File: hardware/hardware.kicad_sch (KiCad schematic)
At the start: 126 parts, among them J1 Conn_01x04_Pin, J2 Conn_01x04_Pin, J3 Conn_01x04_Pin, J4 Conn_01x04_Pin, J5 Conn_01x04_Pin, J6 Conn_01x04_Pin, J7 Conn_01x04_Pin, U1 DRV8825PWPR, U2 DRV8825PWPR, U3 DRV8825PWPR, U4 DRV8825PWPR, U5 DRV8825PWPR, U6 DRV8825PWPR, U7 DRV8825PWPR

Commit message: add relay + mcu schematic
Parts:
- removed C16, C20: 100n, Capacitor_SMD:CP_Elec_6.3x5.7, symbol Device:C_Polarized
- removed C22: 0.1u, Capacitor_SMD:C_0603_1608Metric, symbol Device:C_Small
- removed C23: 0.47u, Capacitor_SMD:C_0603_1608Metric, symbol Device:C_Small
- removed TP1, TP10, TP11, TP12, TP13, TP14, TP15, TP16, TP17, TP18, TP19, TP2, TP20, TP21, TP22, TP23, TP24, TP25, TP26, TP27, TP28, TP3, TP4, TP5, TP6, TP7, TP8, TP9: TestPoint, TestPoint:TestPoint_Pad_1.5x1.5mm, symbol Connector:TestPoint
- added C16: 0.1u, Capacitor_SMD:C_0603_1608Metric, symbol Device:C_Small
- added C20: 0.47u, Capacitor_SMD:C_0603_1608Metric, symbol Device:C_Small
- added C22, C23: 100n, Capacitor_SMD:CP_Elec_6.3x5.7, symbol Device:C_Polarized
- added D1, D2: 1N4001, Diode_THT:D_DO-41_SOD81_P10.16mm_Horizontal, symbol Diode:1N4001
- added J10, J8: Conn_01x03, symbol Connector_Generic:Conn_01x03
- added J9: Jack-DC, symbol Connector:Jack-DC
- added K1, K2: RAYEX-L90, Relay_THT:Relay_SPDT_Omron-G5LE-1, symbol Relay:RAYEX-L90
- added Q1, Q2: Q_NPN, Package_TO_SOT_SMD:TSOT-23_HandSoldering, symbol Device:Q_NPN
- added R29, R32: 10K, Resistor_SMD:R_0603_1608Metric, symbol Device:R_Small
- added R30, R31: 680, Resistor_SMD:R_0603_1608Metric, symbol Device:R_Small
- added U8: ATmega2560-16A, Package_QFP:TQFP-100_14x14mm_P0.5mm, symbol MCU_Microchip_ATmega:ATmega2560-16A
- C14: value 0.1u -> 10n
- C15: value 0.47u -> 10n
- C17: value 10n -> 0.1u
- C21: value 10n -> 0.47u
- R15: value 1M -> 0.10
- R16: value 10K -> 0.10
- R20, R3: value 10K -> 1M
- R21: value 0.10 -> 1M
- R22: value 0.10 -> 10K
- R23, R4: value 1M -> 10K
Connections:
- net +3.3V: now also C21.2, C20.2; no longer C15.2
- net GND: now also C21.1, R15.2, R16.2, C20.1, C22.2, C23.2, J9.2, Q1.E, Q2.E, R29.2, R32.2; no longer C15.1, R21.2, R22.2
- net VBUS: now also R22.2, R23.2, R4.2; no longer R16.2, R20.2, R3.2
- net at R8.1: now also U2.18 (NFAULT); no longer U1.18 (NFAULT)
- net at C2.2, U1.3 (VCP): now also R3.1; no longer R7.1
- net at U6.2 (CP2): now also C15.1; no longer C21.1
- net at U6.1 (CP1): now also C15.2; no longer C21.2
- net at U2.8 (BOUT2): now also J2.1 (Pin_1); no longer J4.1 (Pin_1)
- net at U2.10 (BOUT1): now also J2.2 (Pin_2); no longer J4.2 (Pin_2)
- net at U2.5 (AOUT1): now also J2.3 (Pin_3); no longer J4.3 (Pin_3)
- net at U2.7 (AOUT2): now also J2.4 (Pin_4); no longer J4.4 (Pin_4)
- net at U5.18 (NFAULT): now also R23.1; no longer R20.1
- net at JP12.2 (C): now also U6.24 (MODE0); no longer U4.26 (MODE2)
- net at U6.9 (ISENB): now also R18.1; no longer R22.1
- net at U4.9 (ISENB): now also R16.1; no longer R14.1
- net at JP15.2 (C): now also U6.25 (MODE1); no longer U5.26 (MODE2)
- net at J3.1 (Pin_1): now also U3.8 (BOUT2); no longer U4.8 (BOUT2)
- net at J3.2 (Pin_2): now also U3.10 (BOUT1); no longer U4.10 (BOUT1)
- net at J3.3 (Pin_3): now also U3.5 (AOUT1); no longer U4.5 (AOUT1)
- net at J3.4 (Pin_4): now also U3.7 (AOUT2); no longer U4.7 (AOUT2)
- net at U4.18 (NFAULT): now also R22.1; no longer R16.1
- net at JP11.2 (C): now also U5.24 (MODE0); no longer U4.25 (MODE1)
- net at C6.2, U2.3 (VCP): now also R7.1; no longer R4.1
- net at JP16.2 (C): now also U4.26 (MODE2); no longer U6.24 (MODE0)
- net at R21.1: now also C18.2, U6.3 (VCP); no longer U6.6 (ISENA)
- net at U5.1 (CP1): now also C14.2; no longer C17.2
- net at U5.2 (CP2): now also C14.1; no longer C17.1
- net at JP13.2 (C): now also U4.25 (MODE1); no longer U5.24 (MODE0)
- net at R17.1: now also U5.9 (ISENB); no longer U5.6 (ISENA)
- net at JP17.2 (C): now also U5.26 (MODE2); no longer U6.25 (MODE1)
- net +BATT renamed +12V
- net +12V: now also C17.1, R20.2, R21.2, R3.2, C16.1, C22.1, C23.1, D1.1 (K), D2.1 (K), J9.1, K1.A1, K2.A1; no longer C14.1, R15.2, R23.2, R4.2
- new net: Q2.B, R31.2, R32.1
- new net: D2.2 (A), K2.A2, Q2.C
- new net: Q1.B, R29.1, R30.2
- new net: J8.2 (Pin_2), K1.11A, K1.11B
- new net: J8.1 (Pin_1), K1.12
- new net: J8.3 (Pin_3), K1.14
- new net: D1.2 (A), K1.A2, Q1.C
- new net: J10.2 (Pin_2), K2.11A, K2.11B
- new net: J10.1 (Pin_1), K2.12
- new net: J10.3 (Pin_3), K2.14
- new net: C17.2, R20.1, U5.3 (VCP)
- new net: R14.1, U5.6 (ISENA)
- new net: U8.10 (VCC), U8.31 (VCC), U8.61 (VCC), U8.80 (VCC)
- new net: U8.11 (GND), U8.32 (GND), U8.62 (GND), U8.81 (GND), U8.99 (GND)
- new net: R4.1, U1.18 (NFAULT)
- new net: C16.2, R19.1, U4.3 (VCP)
- new net: J4.1 (Pin_1), U4.8 (BOUT2)
- new net: J4.2 (Pin_2), U4.10 (BOUT1)
- new net: J4.3 (Pin_3), U4.5 (AOUT1)
- new net: J4.4 (Pin_4), U4.7 (AOUT2)
- new net: R15.1, U6.6 (ISENA)
- new net RELAY_1: R31.1
- new net RELAY_2: R30.1

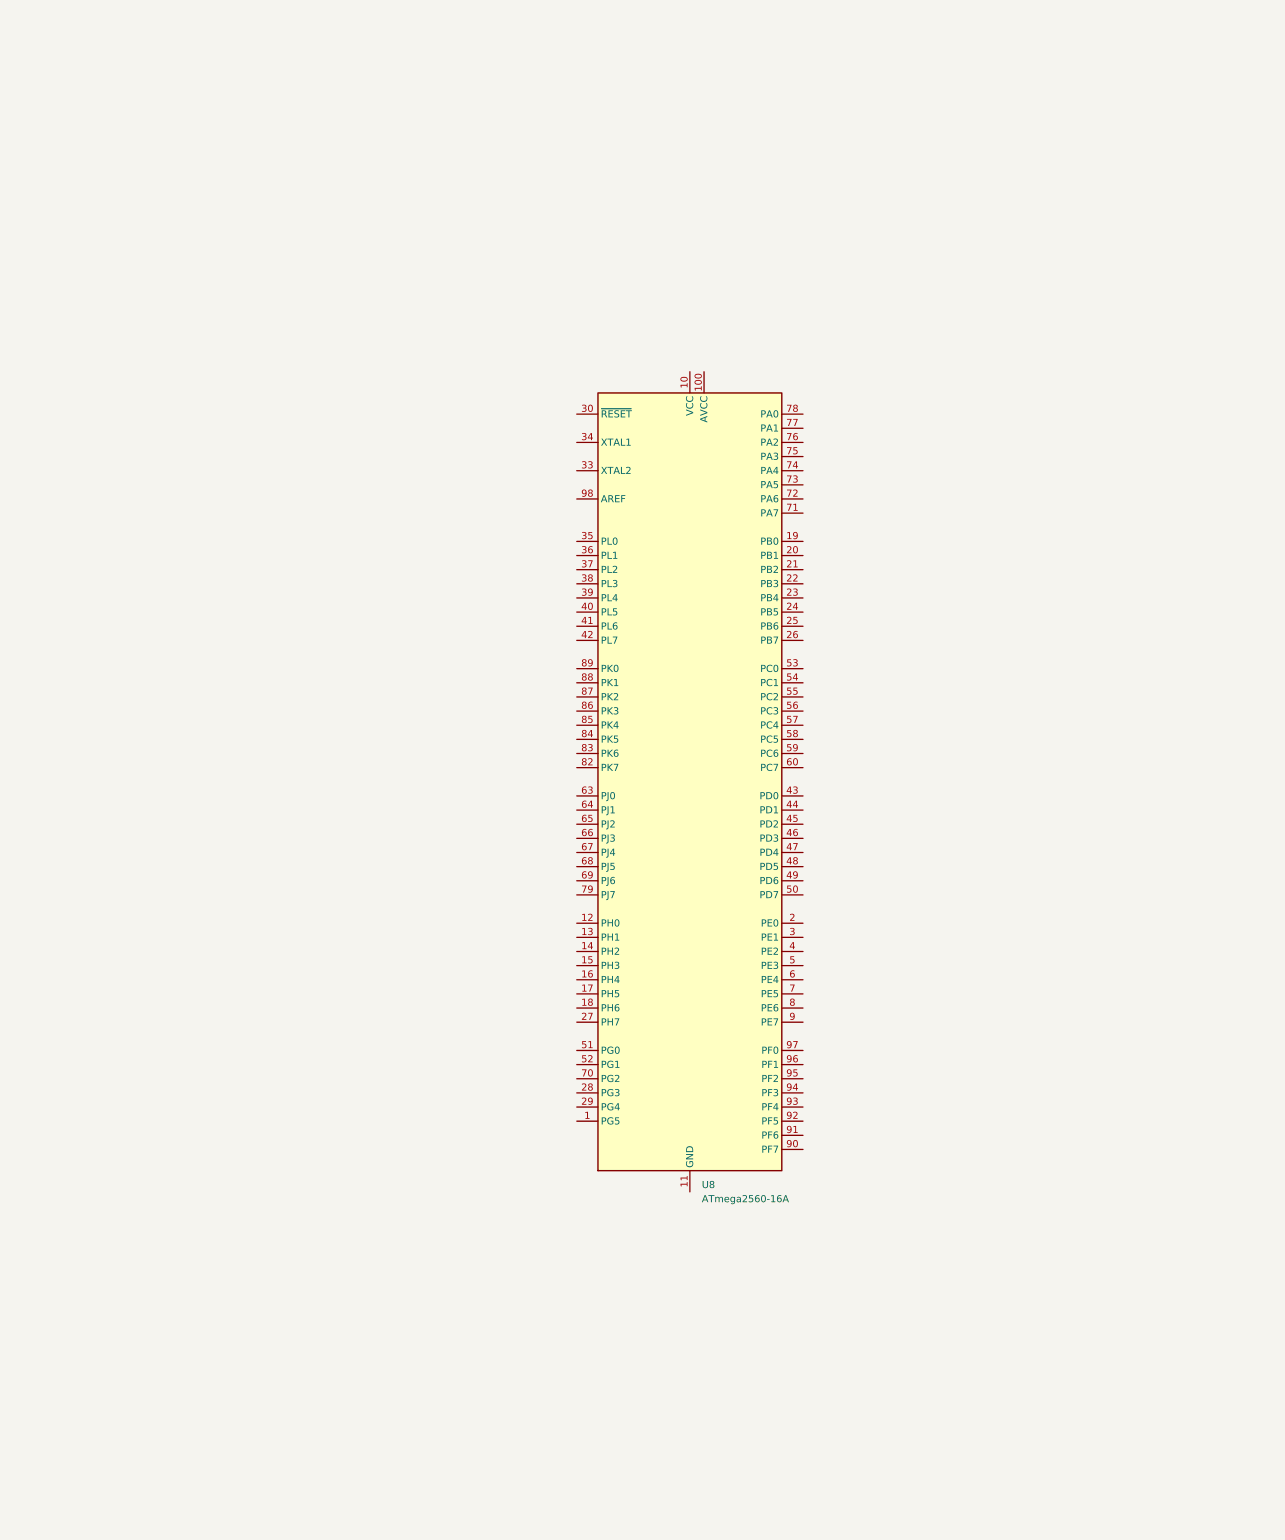
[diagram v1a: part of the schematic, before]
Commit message: add connector + uart to usb + avr isp programming schematic
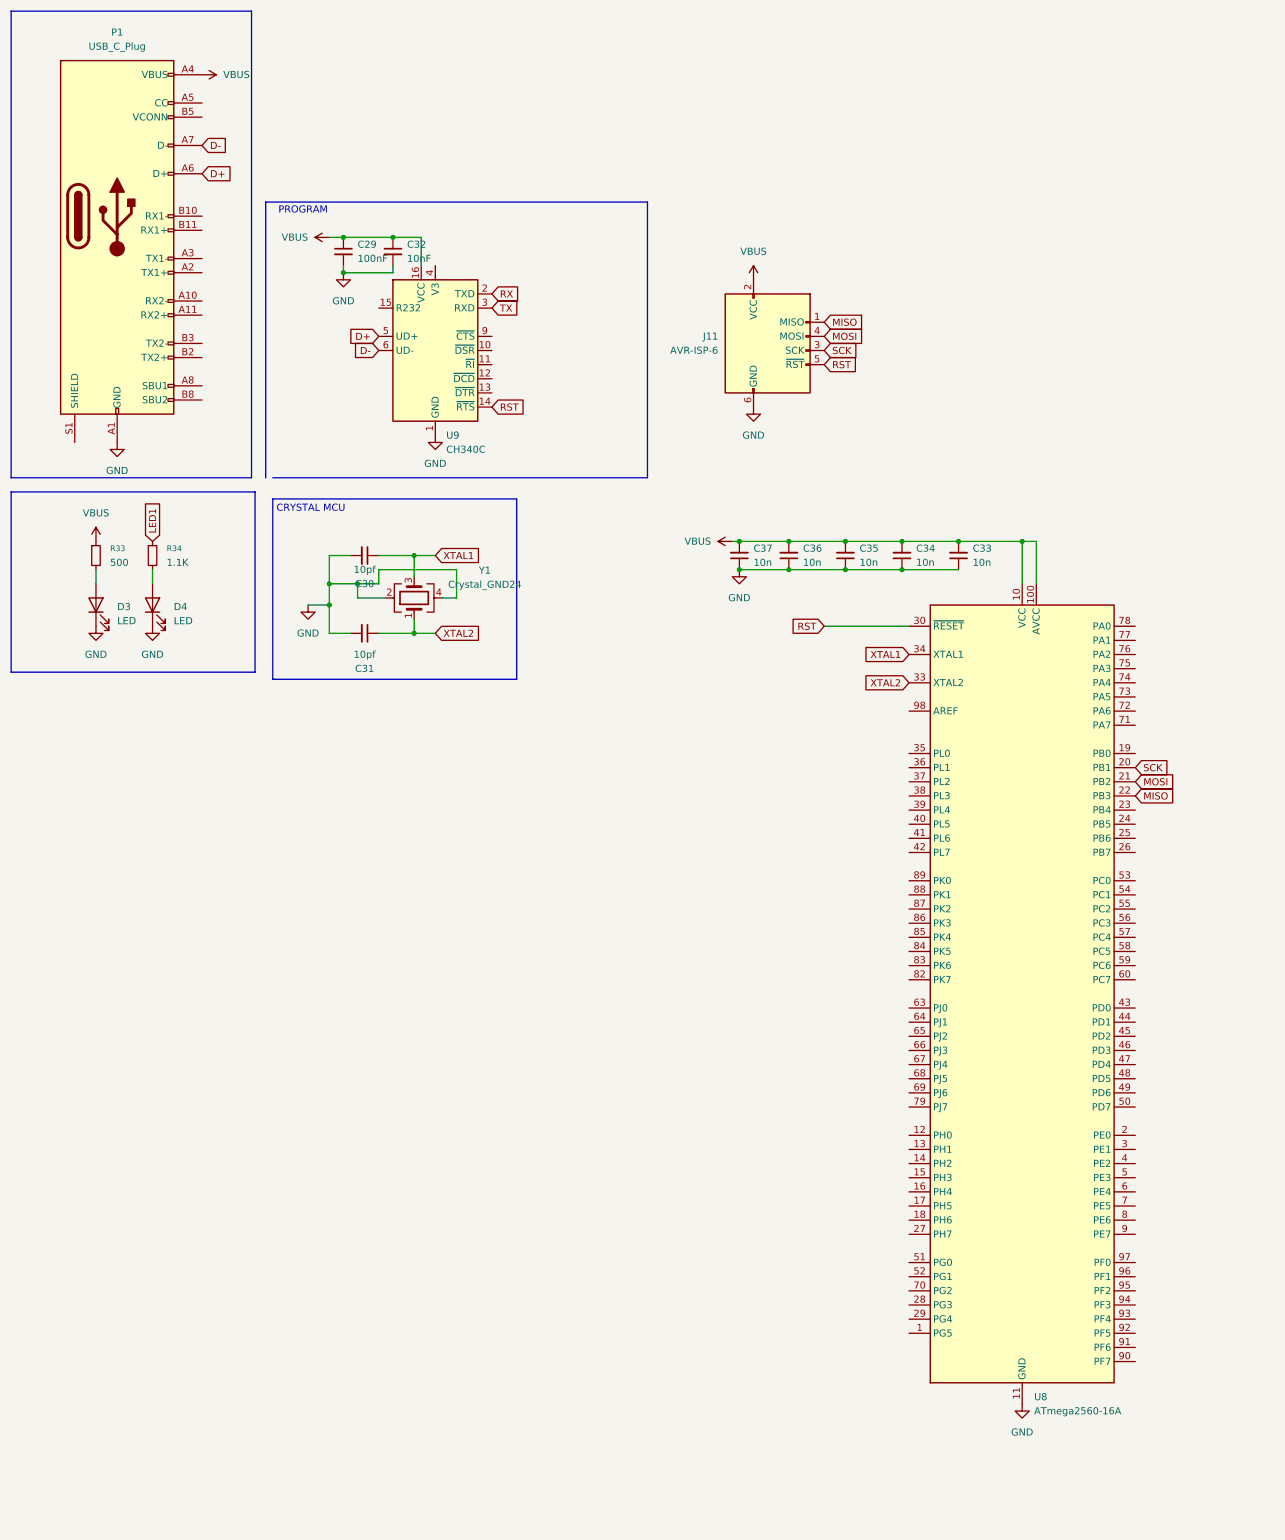
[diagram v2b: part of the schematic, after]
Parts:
- added C29: 100nF, Capacitor_SMD:C_0603_1608Metric, symbol Device:C_Small
- added C30, C31: 10pf, Capacitor_SMD:C_0603_1608Metric, symbol Device:C_Small
- added C32: 10nF, Capacitor_SMD:C_0603_1608Metric, symbol Device:C_Small
- added C33, C34, C35, C36, C37: 10n, Capacitor_SMD:C_0603_1608Metric, symbol Device:C_Small
- added D3, D4: LED, LED_SMD:LED_0603_1608Metric, symbol Device:LED
- added J11: AVR-ISP-6, Connector_PinHeader_2.54mm:PinHeader_2x03_P2.54mm_Vertical, symbol Connector:AVR-ISP-6
- added P1: USB_C_Plug, Connector_USB:USB_C_Receptacle_GCT_USB4105-xx-A_16P_TopMnt_Horizontal, symbol Connector:USB_C_Plug
- added R33: 500, Resistor_SMD:R_0603_1608Metric, symbol Device:R_Small
- added R34: 1.1K, Resistor_SMD:R_0603_1608Metric, symbol Device:R_Small
- added U9: CH340C, Package_SO:SOIC-16_3.9x9.9mm_P1.27mm, symbol Interface_USB:CH340C
- added Y1: Crystal_GND24, Crystal:Crystal_SMD_3225-4Pin_3.2x2.5mm, symbol Device:Crystal_GND24
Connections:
- net GND: now also U8.11 (GND), U8.32 (GND), U8.62 (GND), U8.81 (GND), U8.99 (GND), C29.2, C30.2, C31.2, C32.2, C33.1, C34.1, C35.1, C36.1, C37.1, D3.1 (K), D4.1 (K), J11.6 (GND), P1.A1 (GND), P1.A12 (GND), P1.B1 (GND), P1.B12 (GND), U9.1 (GND), Y1.2, Y1.4
- net VBUS: now also U8.10 (VCC), U8.100 (AVCC), U8.31 (VCC), U8.61 (VCC), U8.80 (VCC), C29.1, C32.1, C33.2, C34.2, C35.2, C36.2, C37.2, J11.2 (VCC), P1.A4 (VBUS), P1.A9 (VBUS), P1.B4 (VBUS), P1.B9 (VBUS), R33.1, U9.16 (VCC)
- net SCK: now reaches U8.20 (PB1)
- net SCK: now also J11.3 (SCK)
- net MOSI: now reaches U8.21 (PB2)
- net MOSI: now also J11.4 (MOSI)
- net MISO: now reaches U8.22 (PB3)
- net MISO: now also J11.1 (MISO)
- net RST: now reaches U8.30 (~{RESET})
- net RST: now also J11.5 (~{RST}), U9.14 (~{RTS})
- net XTAL2: now reaches U8.33 (XTAL2)
- net XTAL2: now also C31.1, Y1.1
- net XTAL1: now reaches U8.34 (XTAL1)
- net XTAL1: now also C30.1, Y1.3
- new net: D3.2 (A), R33.2
- new net: D4.2 (A), R34.2
- new net D+: P1.A6 (D+), U9.5 (UD+)
- new net D-: P1.A7 (D-), U9.6 (UD-)
- new net LED1: R34.1
- new net RX: U9.2 (TXD)
- new net TX: U9.3 (RXD)
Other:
- note added: "CRYSTAL MCU"
- note added: "PROGRAM"
- moved on the sheet: U8

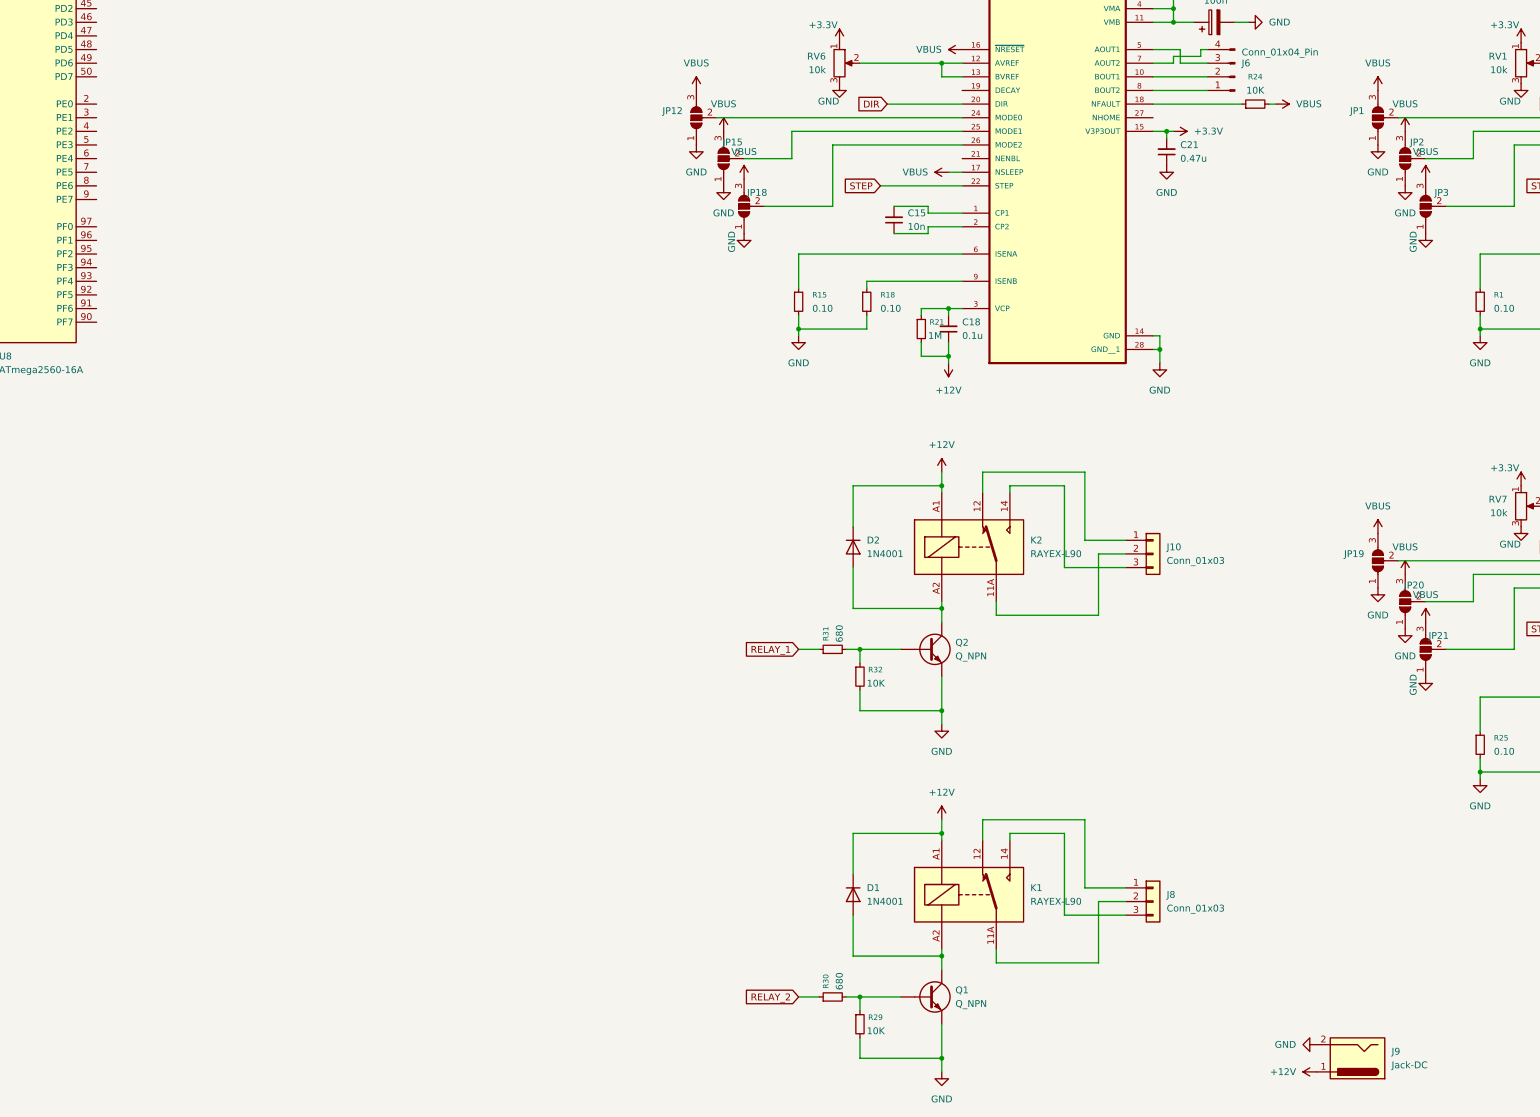
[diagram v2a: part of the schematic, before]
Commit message: add pcb and footprints components
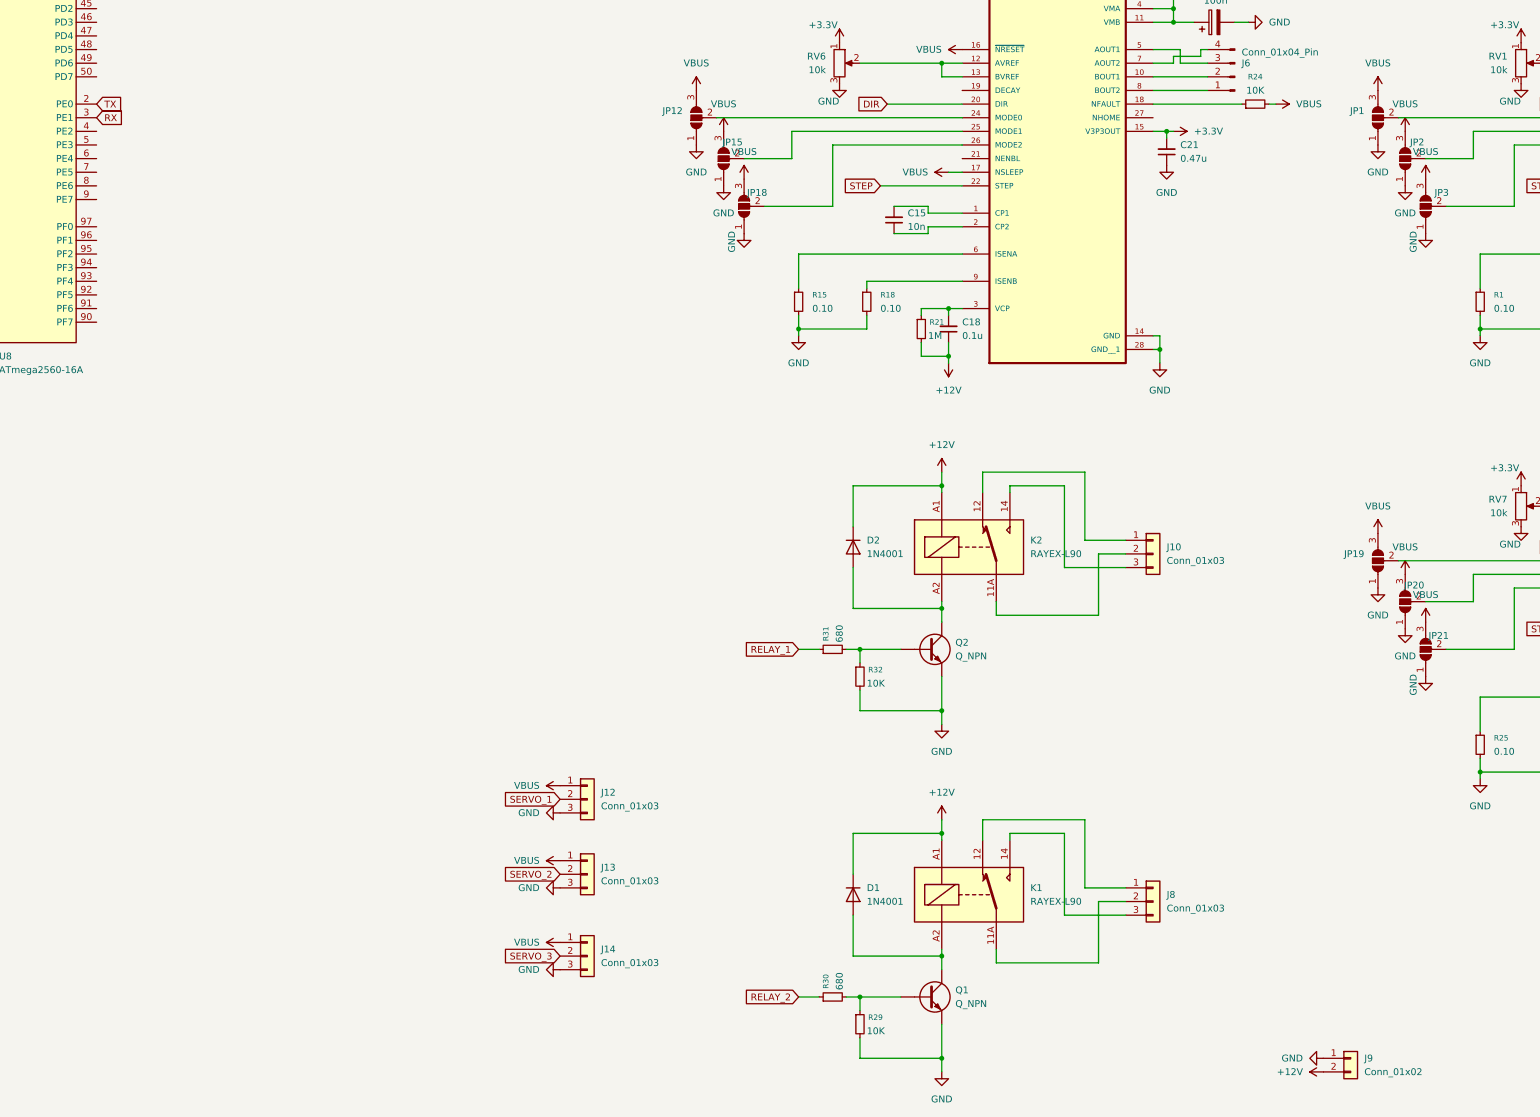
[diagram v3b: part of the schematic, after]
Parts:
- removed J9: Jack-DC, symbol Connector:Jack-DC
- added J12, J13, J14: Conn_01x03, symbol Connector_Generic:Conn_01x03
- added J9: Conn_01x02, TerminalBlock_Phoenix:TerminalBlock_Phoenix_PT-1,5-2-3.5-H_1x02_P3.50mm_Horizontal, symbol Connector_Generic:Conn_01x02
- J10, J8: footprint (none) -> TerminalBlock_Phoenix:TerminalBlock_Phoenix_MPT-0,5-3-2.54_1x03_P2.54mm_Horizontal
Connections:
- net +12V: now also J9.2 (Pin_2)
- net GND: now also J12.3 (Pin_3), J13.3 (Pin_3), J14.3 (Pin_3), J9.1 (Pin_1)
- net RX: now also U8.3 (PE1)
- net TX: now also U8.2 (PE0)
- net VBUS: now also J12.1 (Pin_1), J13.1 (Pin_1), J14.1 (Pin_1)
- new net SERVO_1: J12.2 (Pin_2)
- new net SERVO_2: J13.2 (Pin_2)
- new net SERVO_3: J14.2 (Pin_2)
